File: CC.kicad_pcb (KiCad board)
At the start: 2 copper layers, 75 x 34 mm, 46 parts, among them J1 Conn_01x02_Female, J2 Conn_02x20_Odd_Even, Q1 Q_DUAL_NPN, SW1 SW-2P, U1 CH9328, U2 CP2102N-A01-GQFN28, U3 ESP32-WROOM-32D, U4 AMS1117-3.3, U5 BL1530-DPDT

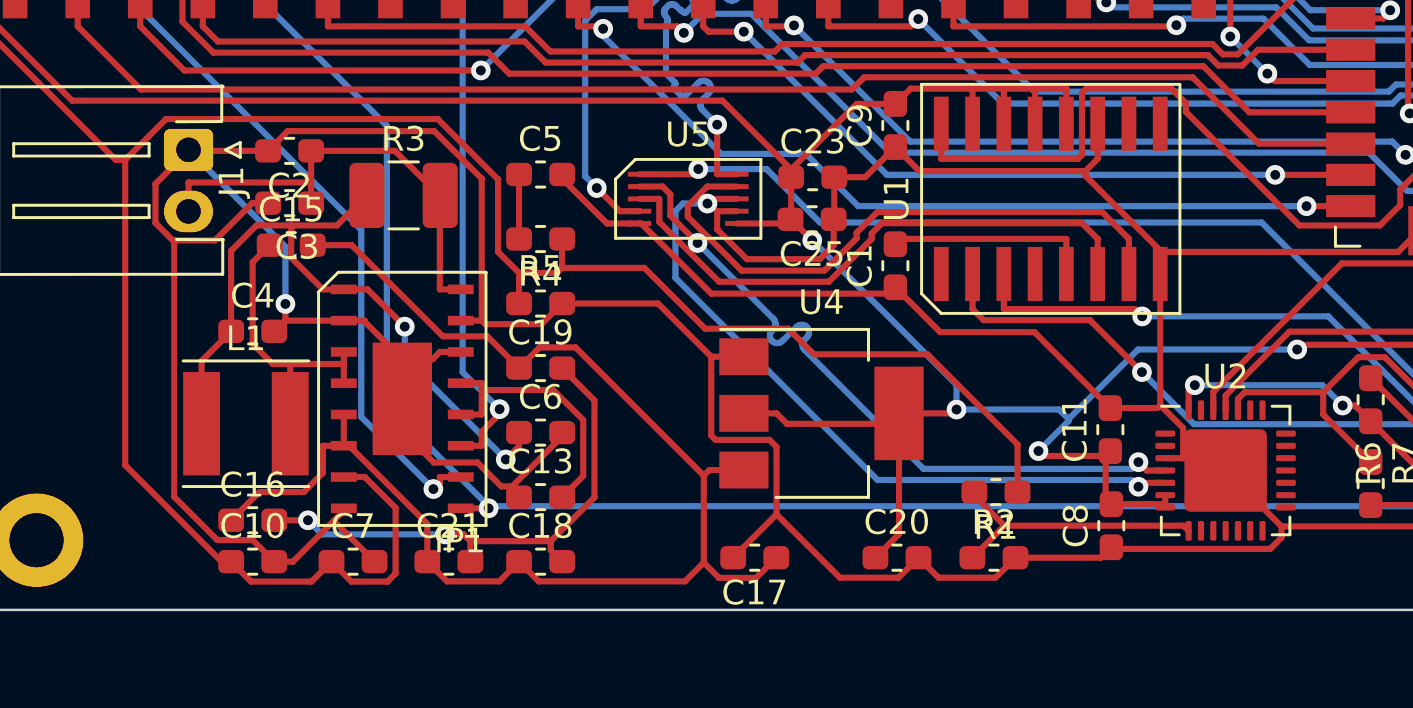
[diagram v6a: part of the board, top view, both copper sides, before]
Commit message: feat: update differential skew
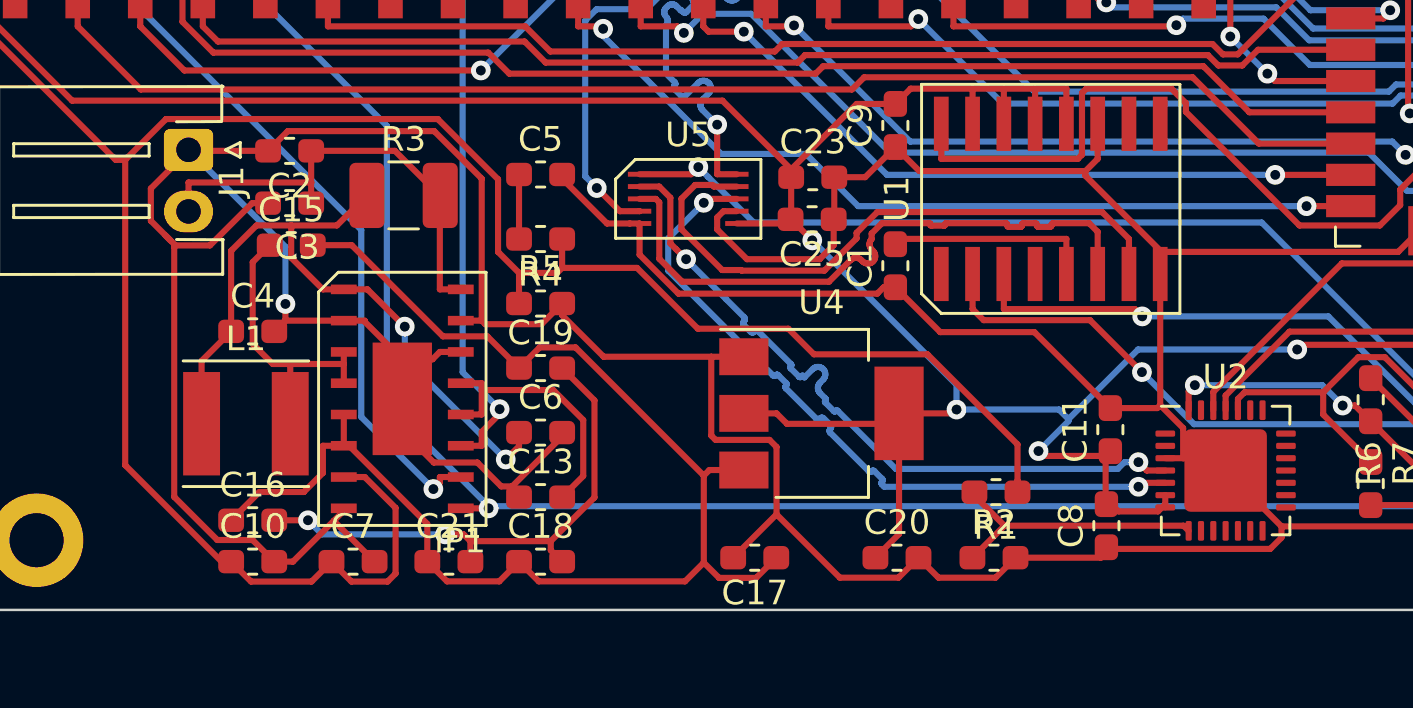
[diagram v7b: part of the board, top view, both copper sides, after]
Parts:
- moved C8 0.20 mm to (76.2, 50.6)
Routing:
- net /KD+: track 23.3 -> 25.6 mm
- net GND: track 351.6 -> 352.9 mm
- net /KD-: track 24.6 -> 25.6 mm
